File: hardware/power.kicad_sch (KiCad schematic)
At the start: 20 parts, among them J1 Conn_01x02, J2 USB4105-GF-A, U3 USBLC6-2SC6, U4 MCP73871, U5 TPS63001DRCR

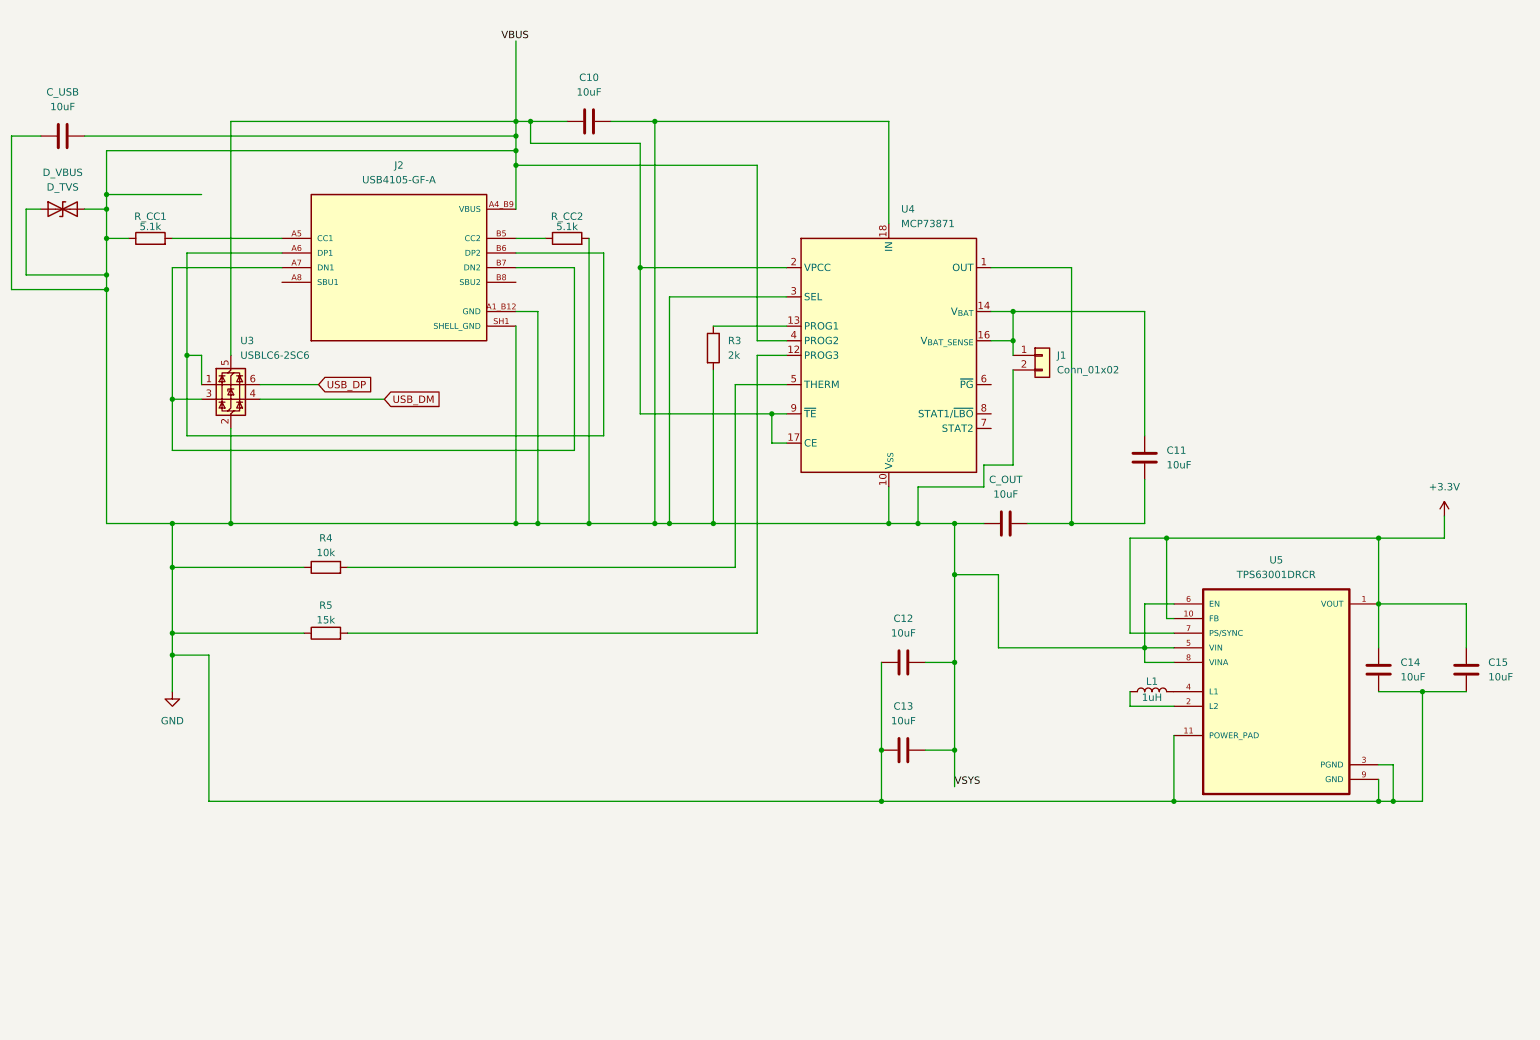
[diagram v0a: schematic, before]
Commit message: add TPS22919 for powering off the radio
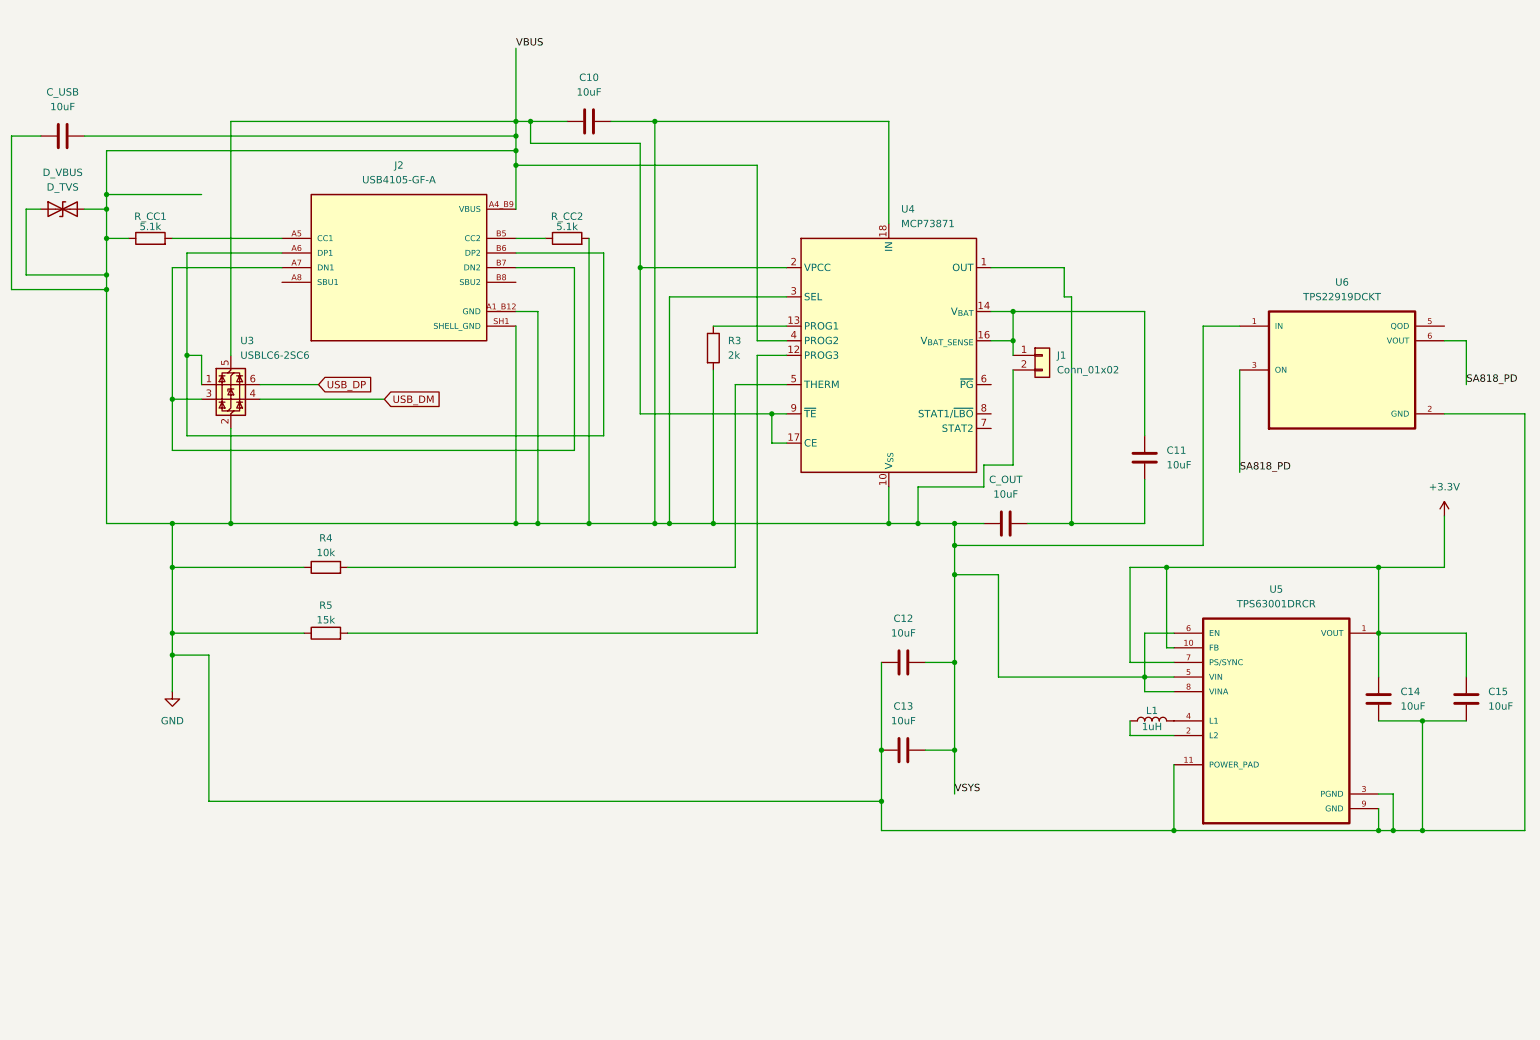
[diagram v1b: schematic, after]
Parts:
- added U6: TPS22919DCKT, TPS22919DCKT:SOT65P210X110-6N, symbol TPS22919DCKT:TPS22919DCKT
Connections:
- net GND: now also U6.1 (IN), U6.2 (GND)
- new net SA818_PD: U6.3 (ON), U6.6 (VOUT)
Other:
- moved on the sheet: C14, C15, L1, U5

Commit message: add battery fuel gauge
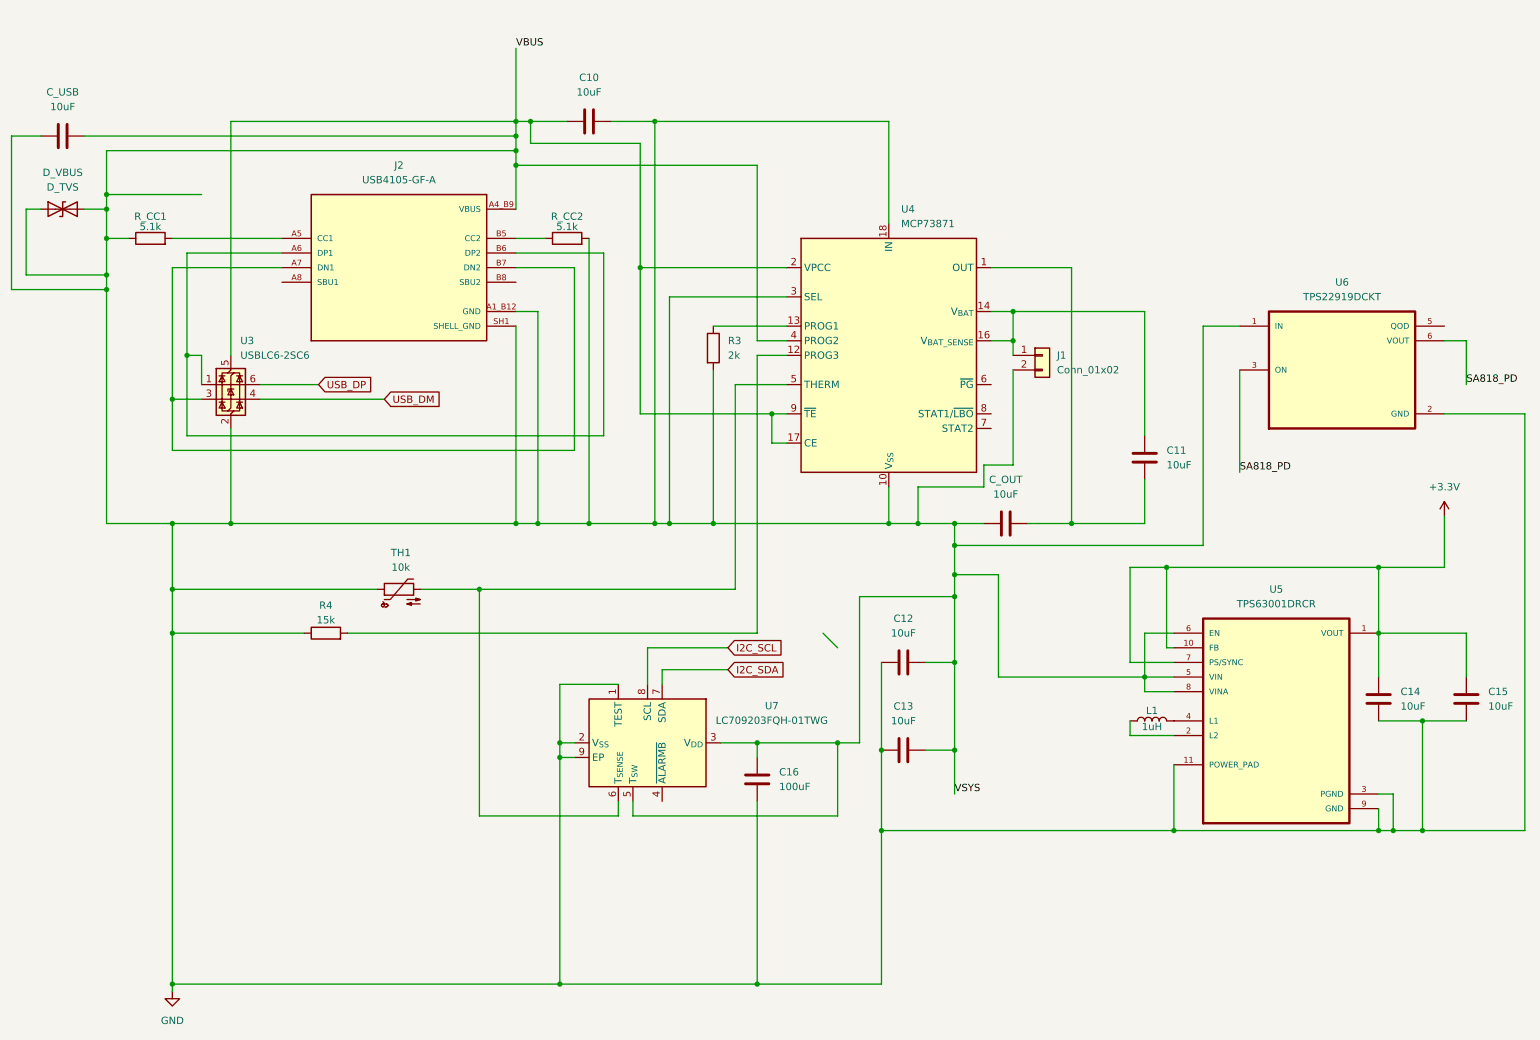
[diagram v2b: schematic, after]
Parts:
- removed R4: 10k, symbol Device:R
- added C16: 100uF, symbol Device:C
- added TH1: 10k, symbol Device:Thermistor_NTC
- added U7: LC709203FQH-01TWG, Package_DFN_QFN:WDFN-8-1EP_4x3mm_P0.65mm_EP2.4x1.8mm, symbol Battery_Management:LC709203FQH-01TWG
- renumbered R5 to R4
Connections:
- net GND: now also C16.1, C16.2, TH1.1, U7.1 (TEST), U7.2 (V_{SS}), U7.3 (V_{DD}), U7.5 (T_{SW}), U7.9 (EP)
- net at U4.5 (THERM): now also TH1.2, U7.6 (T_{SENSE})
- new net I2C_SCL: U7.8 (SCL)
- new net I2C_SDA: U7.7 (SDA)

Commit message: RX Filter
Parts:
- added C17: 100uF, symbol Device:C
- added C18: 10uF, symbol Device:C
- C16: value 100uF -> 100nF
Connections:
- net GND: now also C17.2, C18.2
- net SA818_PD: no longer U6.6 (VOUT)
- new net SA818_VCC: C17.1, C18.1, U6.6 (VOUT)
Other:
- company: (none) -> HRV DEFCON SSTV Badge
- title: (none) -> Power Systems
- moved on the sheet: R4, U6

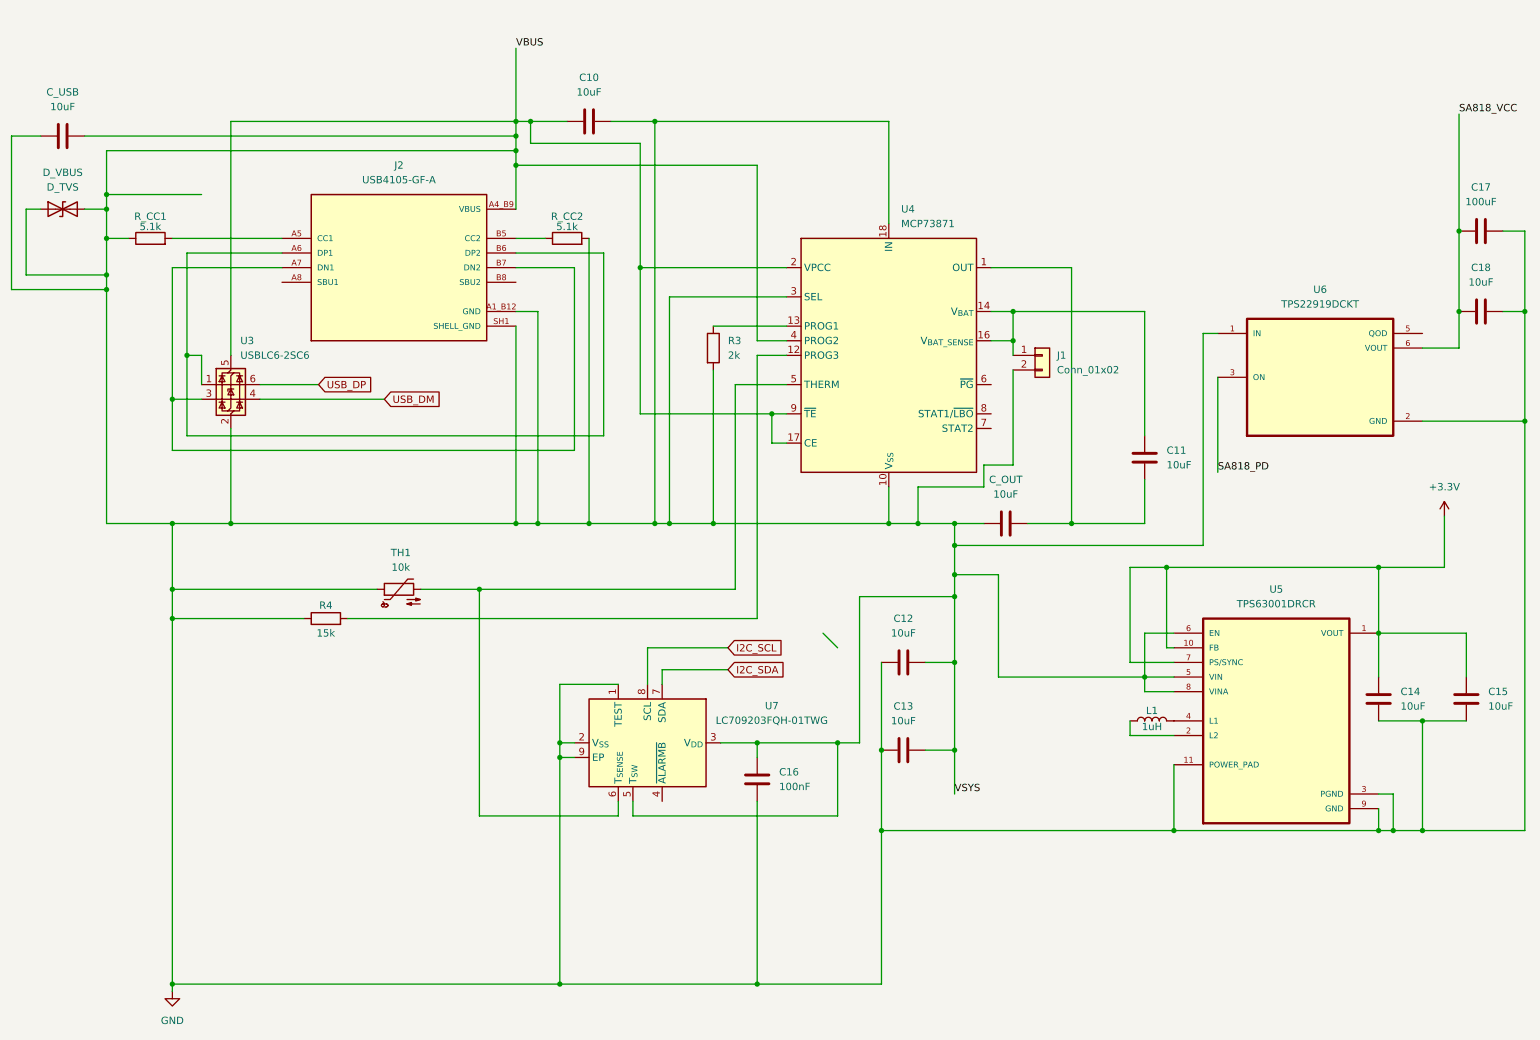
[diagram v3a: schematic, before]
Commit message: all design sheets complete, ERC clean
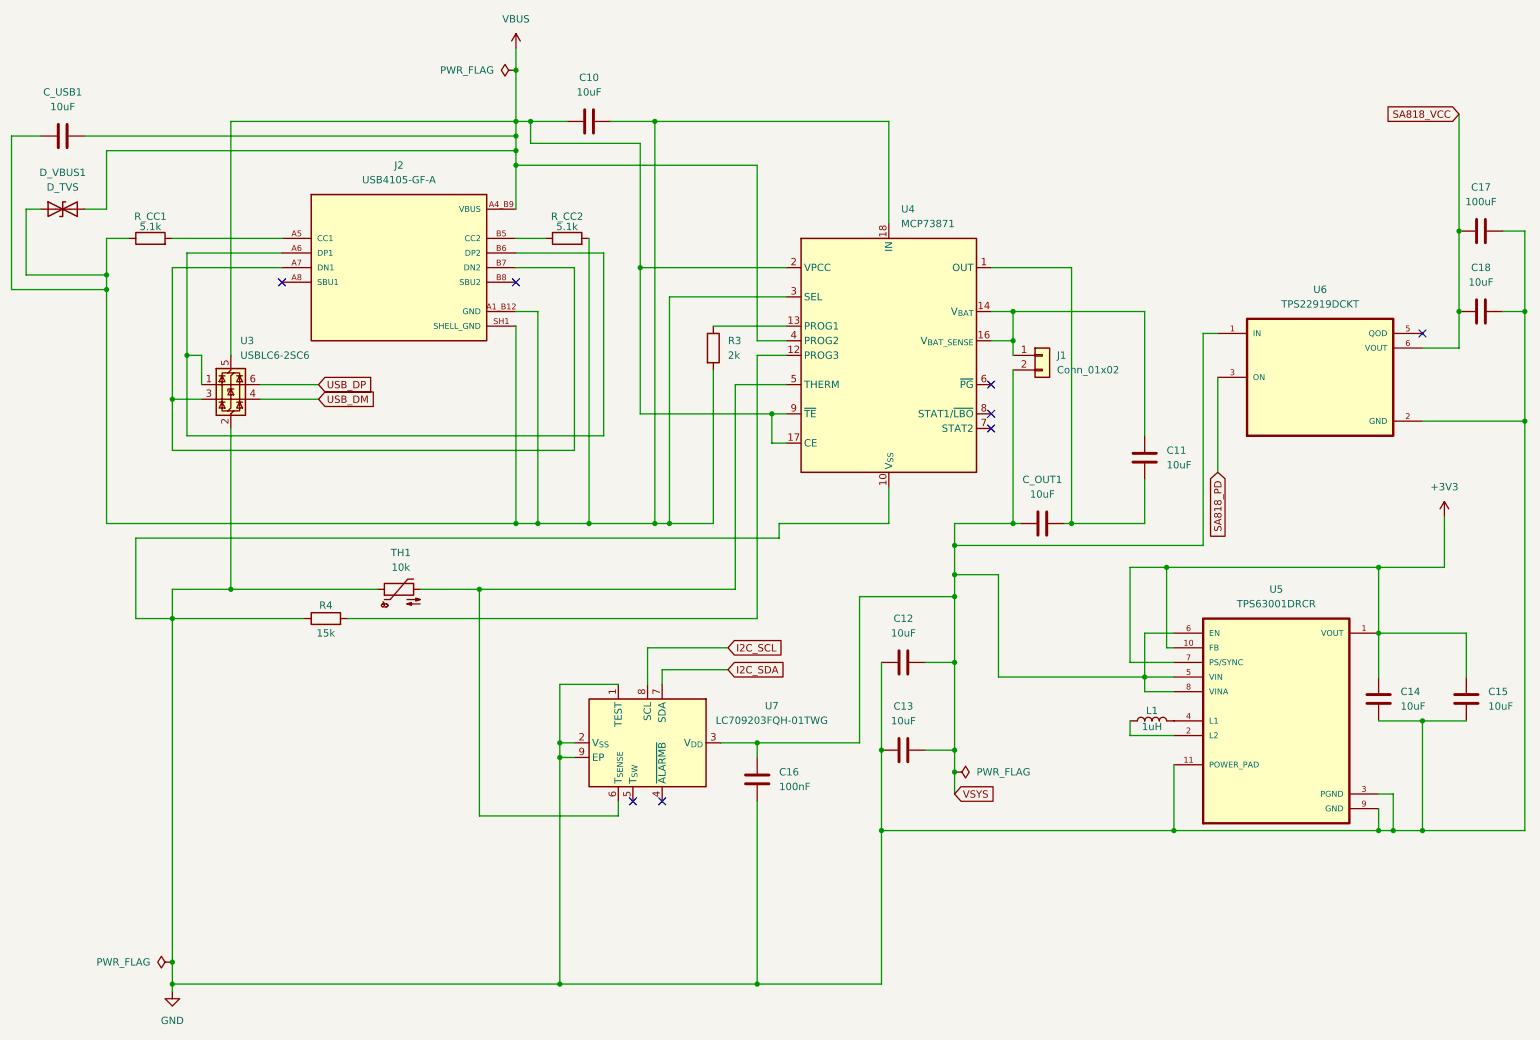
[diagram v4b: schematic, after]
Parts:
- renumbered C_OUT to C_OUT1, C_USB to C_USB1, D_VBUS to D_VBUS1
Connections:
- net GND: no longer C10.1, C12.1, C13.2, C16.1, C_OUT1.1, C_USB1.2, D_VBUS1.2 (A2), J1.2 (Pin_2), J2.A4_B9 (VBUS), J2.B4_A9 (VBUS), U3.5 (VBUS), U4.17 (CE), U4.2 (VPCC), U4.4 (PROG2), U4.9 (~{TE}), U5.5 (VIN), U5.6 (EN), U5.8 (VINA), U6.1 (IN), U7.3 (V_{DD}), U7.5 (T_{SW})
- net +3.3V renamed +3V3
- new net VBUS: C10.1, C_USB1.2, D_VBUS1.2 (A2), J2.A4_B9 (VBUS), J2.B4_A9 (VBUS), U3.5 (VBUS), U4.17 (CE), U4.2 (VPCC), U4.4 (PROG2), U4.9 (~{TE})
- new net VSYS: C12.1, C13.2, C16.1, C_OUT1.1, J1.2 (Pin_2), U5.5 (VIN), U5.6 (EN), U5.8 (VINA), U6.1 (IN), U7.3 (V_{DD})
- no-connect marks 0 -> 8
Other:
- moved on the sheet: C_OUT1
